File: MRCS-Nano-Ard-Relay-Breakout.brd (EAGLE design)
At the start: 99.8 x 68.8 mm, 11 parts, among them CON1 5V PWR, J1 5V PWR, J2 Unused I/O, J4 Outputs

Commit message: files as sent to jlcpcb for 1st run
completion of design
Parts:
- removed J4: Outputs, SPCoast:1X08_LOCK
- removed SENSOR0-3, SENSOR4-7: (no value), SPCoast:1X08_LOCK
- added A3-0, D13-10, D5-2, D9-6: (no value), SPCoast:1X06_LOCK
- added D10, D11, D12, D13: CONNECTOR-M03MOLEX-254-LOCK, SPCoast:MOLEX-1X3_LOCK
- added D10-A3, D2-D9: CONNECTOR-M102MM, SPCoast:1X10-2MM
- added D3-2, D5-4, D7-6, D9-8: (no value), SPCoast:1X04_LOCK
- added U$3: (no value), MRCSLogoTop:MRCSLOGOTOP
- added U$4: (no value), MRCSLogoBtm:MRCSLOGOBTM
- moved U$1 19.1 mm to (50.8, 22.9)
- moved U$2 7.73 mm to (39.4, 52.1)
- moved CON1 5.08 mm to (76.2, 11.4)
- moved J1 3.81 mm to (87.6, 19.1)
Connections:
- removed net A0: SENSOR0-3.8, U$1.A0
- removed net N$1: U$1.A4
- removed net N$2: U$1.D2
- removed net N$20: U$1.D12
- removed net N$21: U$1.D11
- removed net N$22: U$1.D8
- removed net N$24: U$1.D6
- removed net N$25: U$1.D5
- removed net N$6: U$1.D4
- new net A4: J2.6, U$1.A4
- new net A5: J2.5, U$1.A5
- new net A6: J2.4, U$1.A6
- new net A7: J2.3, U$1.A7
- new net N$14: D10-A3.6, D13-10.2, D13.2, U$1.D13
- new net N$18: A3-0.2, D10-A3.2, U$1.A3
- new net N$19: D2-D9.7, D5-2.3, D5-4.3, U$1.D4
- new net N$8: D2-D9.4, D7-6.2, D9-6.4, U$1.D7
- new net N$9: D2-D9.3, D9-6.3, D9-8.3, U$1.D8
- new net RX1: J2.2, U$1.RX1
- new net TX0: J2.1, U$1.TX0
- net 5V: now also A3-0.1, D10-A3.1, D10.1, D11.1, D12.1, D13-10.1, D13.1, D2-D9.1, D3-2.1, D5-2.1, D5-4.1, D7-6.1, D9-6.1, D9-8.1, J2.8; no longer SENSOR0-3.1, SENSOR0-3.3, SENSOR0-3.5, SENSOR0-3.7
- net GND: now also A3-0.6, D10-A3.10, D10.3, D11.3, D12.3, D13-10.6, D13.3, D2-D9.10, D3-2.4, D5-2.6, D5-4.4, D7-6.4, D9-6.6, D9-8.4, J2.7
- net N$10: now also D2-D9.2, D9-6.2, D9-8.2, U$1.D9; no longer SENSOR0-3.4, U$1.A2
- net N$11: now also D10-A3.9, D10.2, D13-10.5, U$1.D10; no longer SENSOR4-7.4
- net N$12: now also D10-A3.8, D11.2, D13-10.4, U$1.D11; no longer SENSOR0-3.2, U$1.A3
- net N$13: now also D10-A3.7, D12.2, D13-10.3, U$1.D12; no longer SENSOR4-7.2
- net N$15: now also A3-0.5, D10-A3.5, U$1.A0; no longer U$1.A6
- net N$16: now also A3-0.4, D10-A3.4, U$1.A1; no longer U$1.A7
- net N$17: now also A3-0.3, D10-A3.3, U$1.A2; no longer SENSOR0-3.6, U$1.A1
- net N$23: now also D2-D9.6, D5-2.2, D5-4.2, U$1.D5; no longer U$1.D7
- net N$3: now also D2-D9.9, D3-2.3, D5-2.5, U$1.D2; no longer U$1.D13
- net N$4: now also D2-D9.8, D3-2.2, D5-2.4
- net N$7: now also D2-D9.5, D7-6.3, D9-6.5, U$1.D6; no longer SENSOR4-7.6, U$1.A5
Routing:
- net N$18: track 0.00 -> 92.8 mm
- net N$3: track 0.00 -> 75.7 mm
- net N$14: track 0.00 -> 67.9 mm
- net N$17: track 21.7 -> 85.8 mm
- net N$19: track 0.00 -> 62.2 mm
- net TX0: track 0.00 -> 60.8 mm
- net A7: track 0.00 -> 59.4 mm
- net RX1: track 0.00 -> 57.5 mm
- net A6: track 0.00 -> 57.5 mm
- net A5: track 0.00 -> 54.0 mm
- net N$8: track 0.00 -> 53.4 mm
- net N$9: track 0.00 -> 52.2 mm
- net A4: track 0.00 -> 51.4 mm
- net N$15: track 19.4 -> 68.2 mm
- net N$4: track 20.8 -> 69.1 mm
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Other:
- board text added: "5VDC"
- board text added: "Arduino Relay Controller Version 1.0 20220319"
- board text added: "D13 D12 D11 D10"
- board text added: "TX0 RX1 A7 A6 A5 A4 GND +5"
- board text added: "V1.0 20200318"
- board text removed: "+GBG+L+L 5NLN5152"
- board text removed: "0+1+2+3+"
- board text removed: "4+5+6+7+"
- board text removed: "5DVC"
- board text removed: "BROWN"
- board text removed: "Grade XING Breakout"
- board text removed: "ORANGE"
- board text removed: "V1.0 20200314"

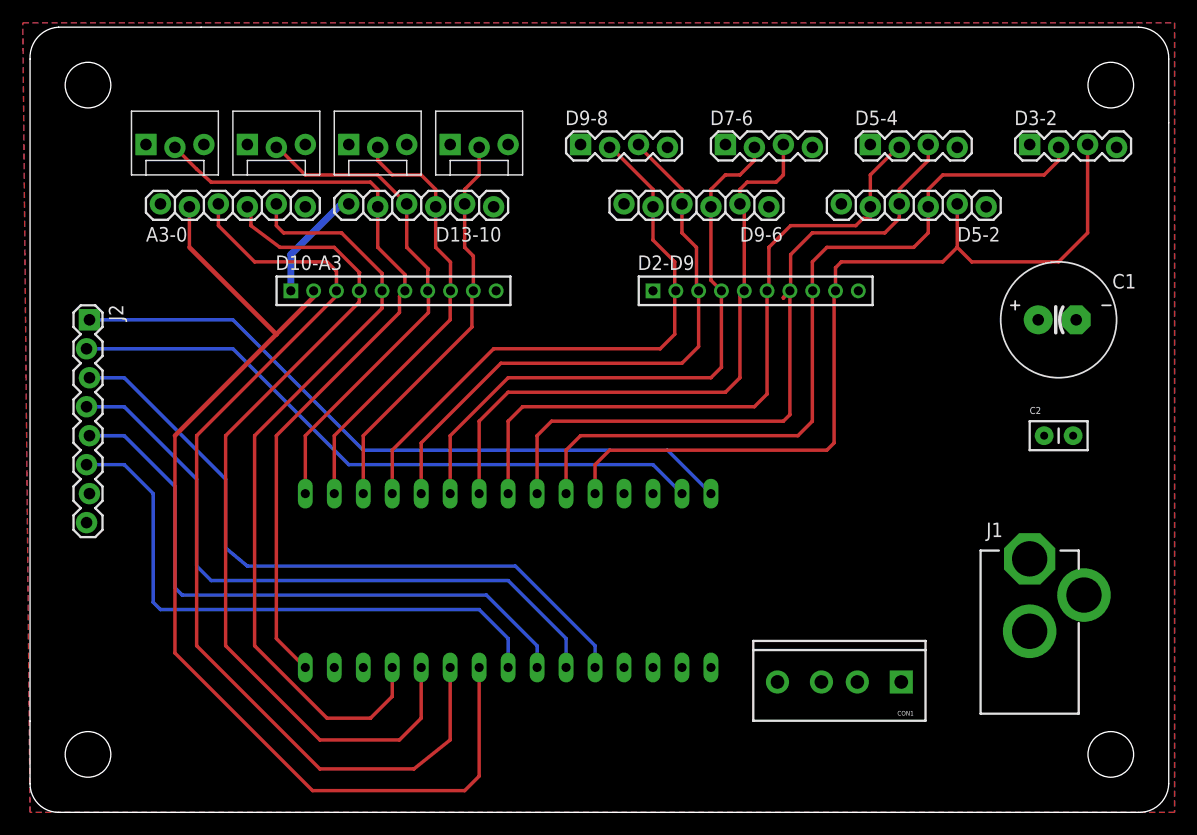
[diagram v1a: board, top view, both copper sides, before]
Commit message: fixed connectors 8 and 16 position Arduino Relays
accidently selected 2mm rather than 2.54mm (0.100) connectors.  Fixed positions of the singlets (different pattern of course).
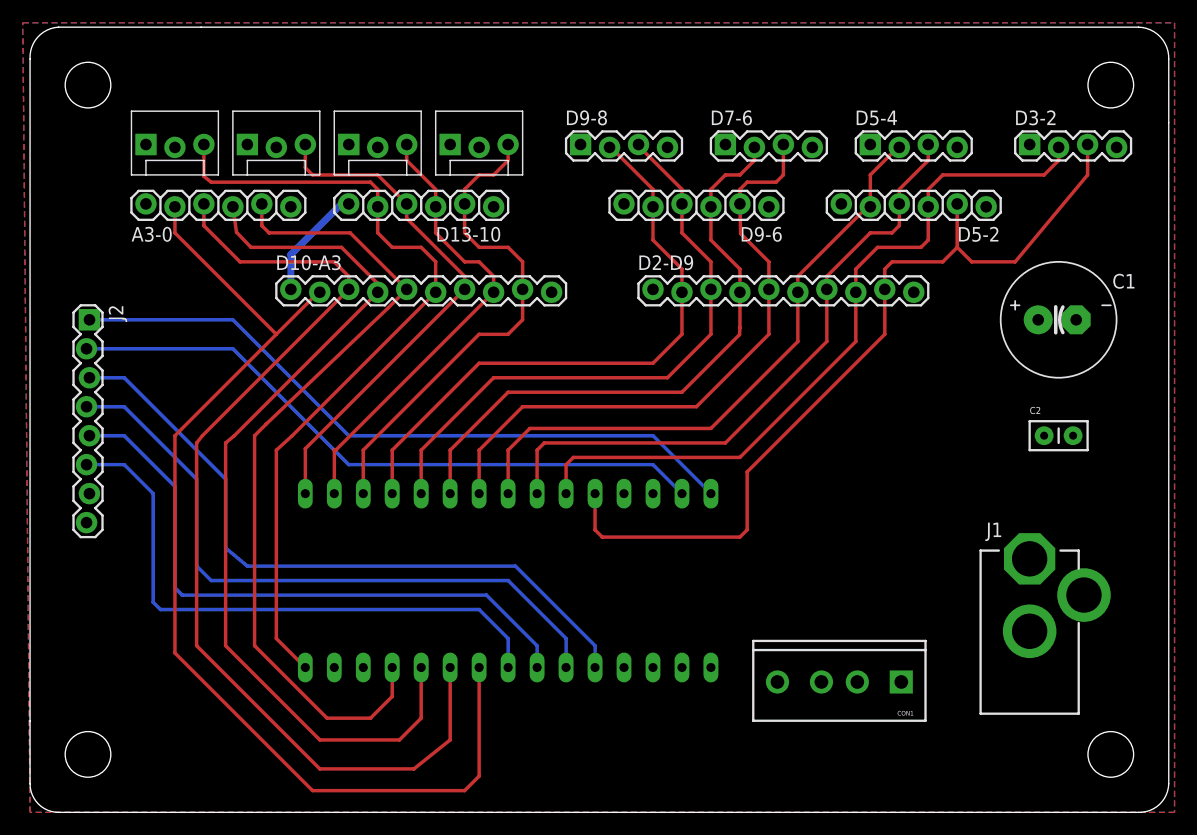
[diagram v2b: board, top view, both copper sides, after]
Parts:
- D10-A3, D2-D9: value CONNECTOR-M102MM -> CONNECTOR-M10LOCK; device SPCoast:1X10-2MM -> SPCoast:1X10_LOCK
- moved U$2 15.3 mm to (45.7, 38.1)
- moved A3-0 1.27 mm to (10.2, 53.3)
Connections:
- net GND: now also D10.2, D11.2, D12.2, D13.2; no longer D10.3, D11.3, D12.3, D13.3
- net N$11: now also D10.3; no longer D10.2
- net N$12: now also D11.3; no longer D11.2
- net N$13: now also D12.3; no longer D12.2
- net N$14: now also D13.3; no longer D13.2
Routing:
- net N$11: track 35.2 -> 43.8 mm
- net N$19: track 62.2 -> 54.7 mm
- net N$23: track 60.3 -> 54.1 mm
- net N$4: track 69.1 -> 64.2 mm
- net N$15: track 68.2 -> 71.9 mm
- net N$16: track 76.2 -> 79.6 mm
- net N$14: track 67.9 -> 70.9 mm
- net N$17: track 85.8 -> 88.3 mm
- net N$12: track 39.0 -> 40.6 mm
- net N$3: track 75.7 -> 74.0 mm
- net N$13: track 44.2 -> 45.5 mm
- net N$10: track 51.7 -> 52.5 mm
- net N$18: track 92.8 -> 93.5 mm
- net N$9: track 52.2 -> 52.7 mm
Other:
- board text added: "+5"
- board text added: "Arduino Relay Controller Version 1.1 20220401"
- board text added: "G"
- board text added: "IN"
- board text removed: "Arduino Relay Controller Version 1.0 20220319"
- board text removed: "V1.0 20200318"
